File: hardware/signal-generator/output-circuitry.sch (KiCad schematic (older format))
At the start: 41 parts, among them U15 MCP4651-502E/ST, U16 AZ431AN-A, U17 AD8021ARZ, U18 MCP4551-103E/MS, U19 AD8021ARZ, U20 AD8021ARZ, U21 AD8021ARZ

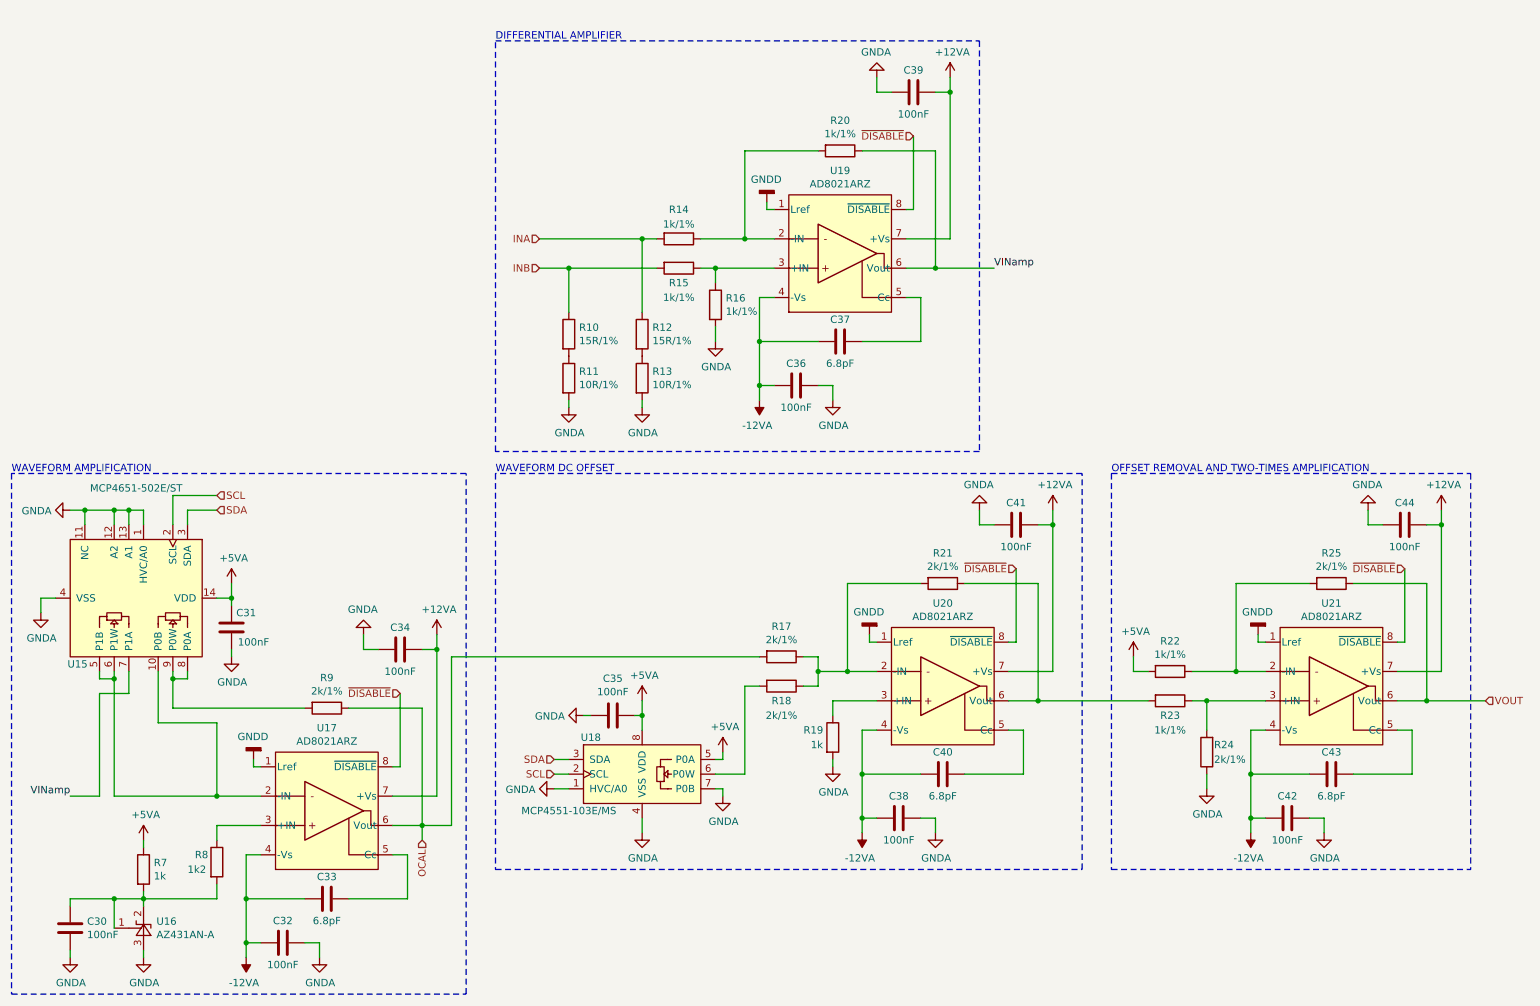
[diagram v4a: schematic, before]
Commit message: [Signal Generator] Rework output circuitry's waveform amplification stage
The previous design of the waveform amplification stage which utilized
a digital potentiometer to regulate gain control was flawed due to the
latter. The digital potentiometer's bandwidth is 2MHz which does not
fulfill the requirements of the circuit - the output stages may need to
accommodate for signals with frequencies in the tens of MHz.

This commit proposes a new design which uses JFET transistors as voltage
controlled variable resistors. In case this new design is unsuccessful,
the gain of the waveform amplification output stage may be regulated via
a mechanical potentiometer.
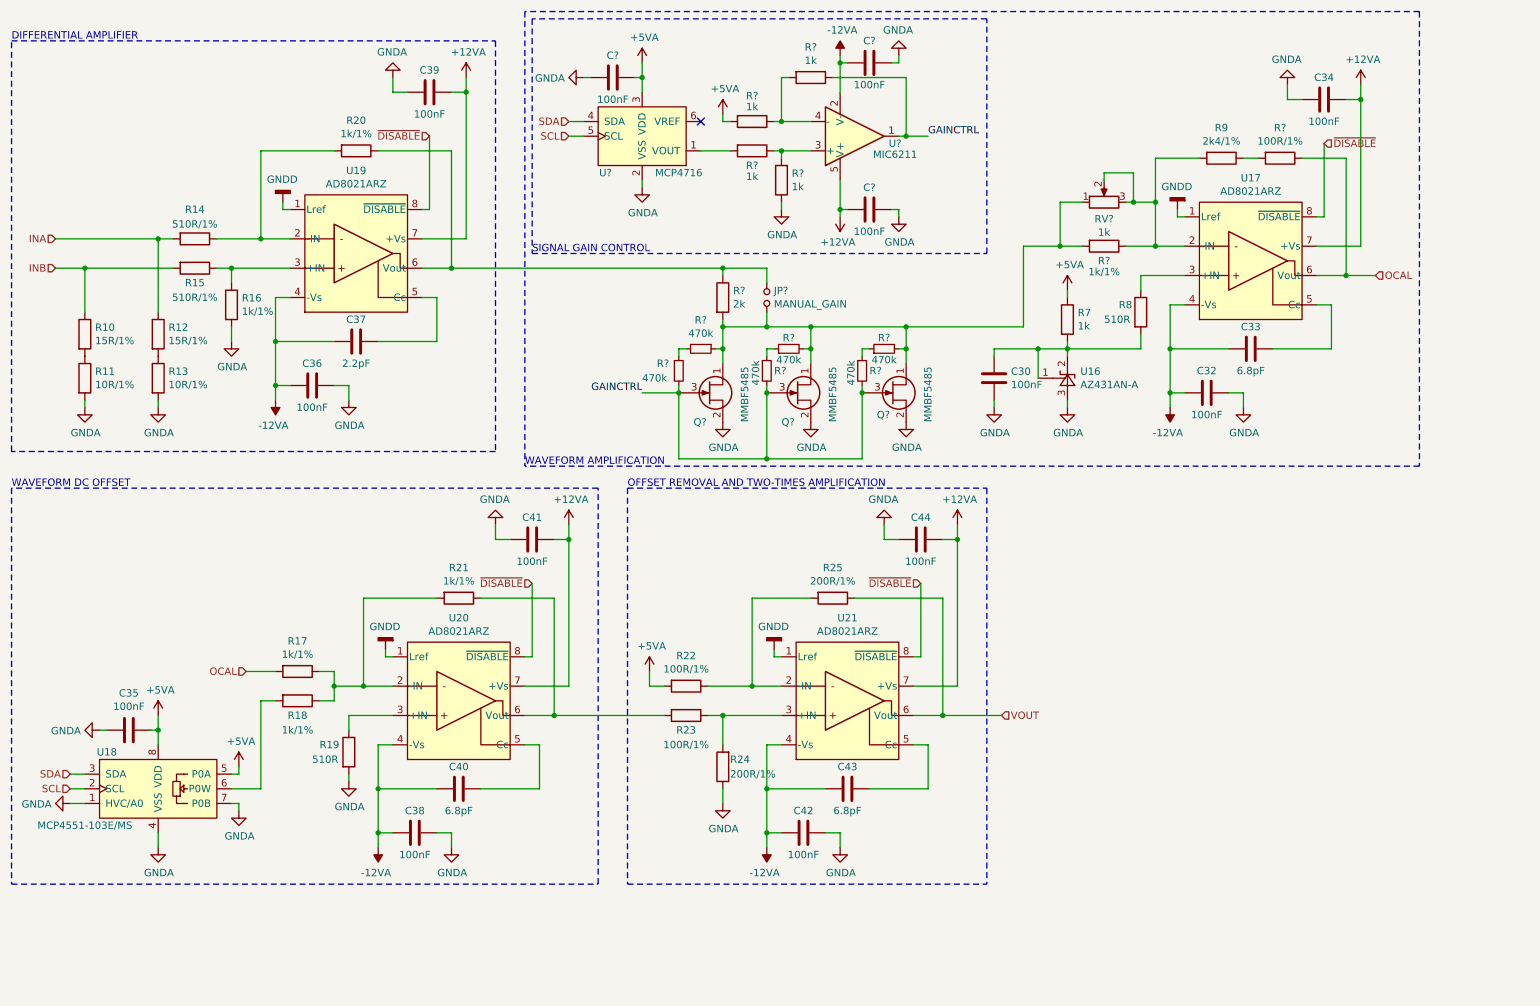
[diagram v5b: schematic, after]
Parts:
- removed C31: 100nF, Capacitors_SMD:C_0805_HandSoldering, symbol Device:C
- removed U15: MCP4651-502E/ST, Housings_SSOP:TSSOP-14_4.4x5mm_Pitch0.65mm, symbol ulib_Digital_Potentiometers:MCP4651-ST
- added C? (x3): 100nF, Capacitors_SMD:C_0805_HandSoldering, symbol Device:C
- added JP?: MANUAL_GAIN, symbol Device:Jumper_NO_Small
- added Q? (x3): MMBF5485, TO_SOT_Packages_SMD:SOT-23_Handsoldering, symbol ulib_MY_Transistor_FET:MMBF5485
- added R?: 1k/1%, symbol Device:R
- added R?: 2k, symbol Device:R
- added R? (x4): 1k, symbol Device:R
- added R?: 100R/1%, Resistors_SMD:R_0805_HandSoldering, symbol Device:R
- added R? (x6): 470k, symbol Device:R_Small
- added RV?: 1k, symbol Device:R_POT
- added U?: MCP4716, TO_SOT_Packages_SMD:SOT-23-6_Handsoldering, symbol ulib_DACs:MCP4716
- added U?: MIC6211, TO_SOT_Packages_SMD:SOT-23-5_HandSoldering, symbol ulib_IC_Amplifiers:MIC6211
- C37: value 6.8pF -> 2.2pF
- R14, R15: value 1k/1% -> 510R/1%
- R17, R18, R21: value 2k/1% -> 1k/1%
- R19: value 1k -> 510R
- R22, R23: value 1k/1% -> 100R/1%
- R24, R25: value 2k/1% -> 200R/1%
- R8: value 1k2 -> 510R
- R9: value 2k/1% -> 2k4/1%
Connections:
- net +12VA: now also C?.2, U?.5 (V+)
- net +5VA: now also C?.1, R?.2, U?.3 (VDD)
- net -12VA: now also C?.2, U?.2 (V-)
- net GNDA: now also C?.1, C?.1, C?.2, Q?.2 (S), Q?.2 (S), Q?.2 (S), R?.1, U?.2 (VSS)
- net OCAL: now also R?.1; no longer R9.1
- net SCL: now also U?.5 (SCL)
- net SDA: now also U?.4 (SDA)
- net at U17.2 (-IN): now also R9.2, R?.1, RV?.2, RV?.3
- net VINamp: no longer names the net of R20.1, U19.6 (Vout)
- net VINamp: now also JP?.1, R?.1
- new net: R9.1, R?.2
- new net: JP?.2, Q?.1 (D), Q?.1 (D), Q?.1 (D), R?.1, R?.2, R?.2, R?.2, R?.2, RV?.1
- new net: R?.2, U?.1 (VOUT)
- new net: R?.1, R?.2, U?.3 (+)
- new net: R?.1, R?.2, U?.4 (-)
- new net: R?.1, R?.2
- new net: R?.1, R?.1 (x2)
- new net GAINCTRL: Q?.3 (G), Q?.3 (G), Q?.3 (G), R?.1, R?.2, R?.2, R?.2, U?.1
- no-connect marks 0 -> 1
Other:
- note added: "SIGNAL GAIN CONTROL"
- moved on the sheet: C30, C32, C33, C34, C35, C36, C37, C38, C39, C40, C41, C42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

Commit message: [Signal Generator] Restore PCB layout with new symbol annotations
The new components have been loaded in the PCB file.
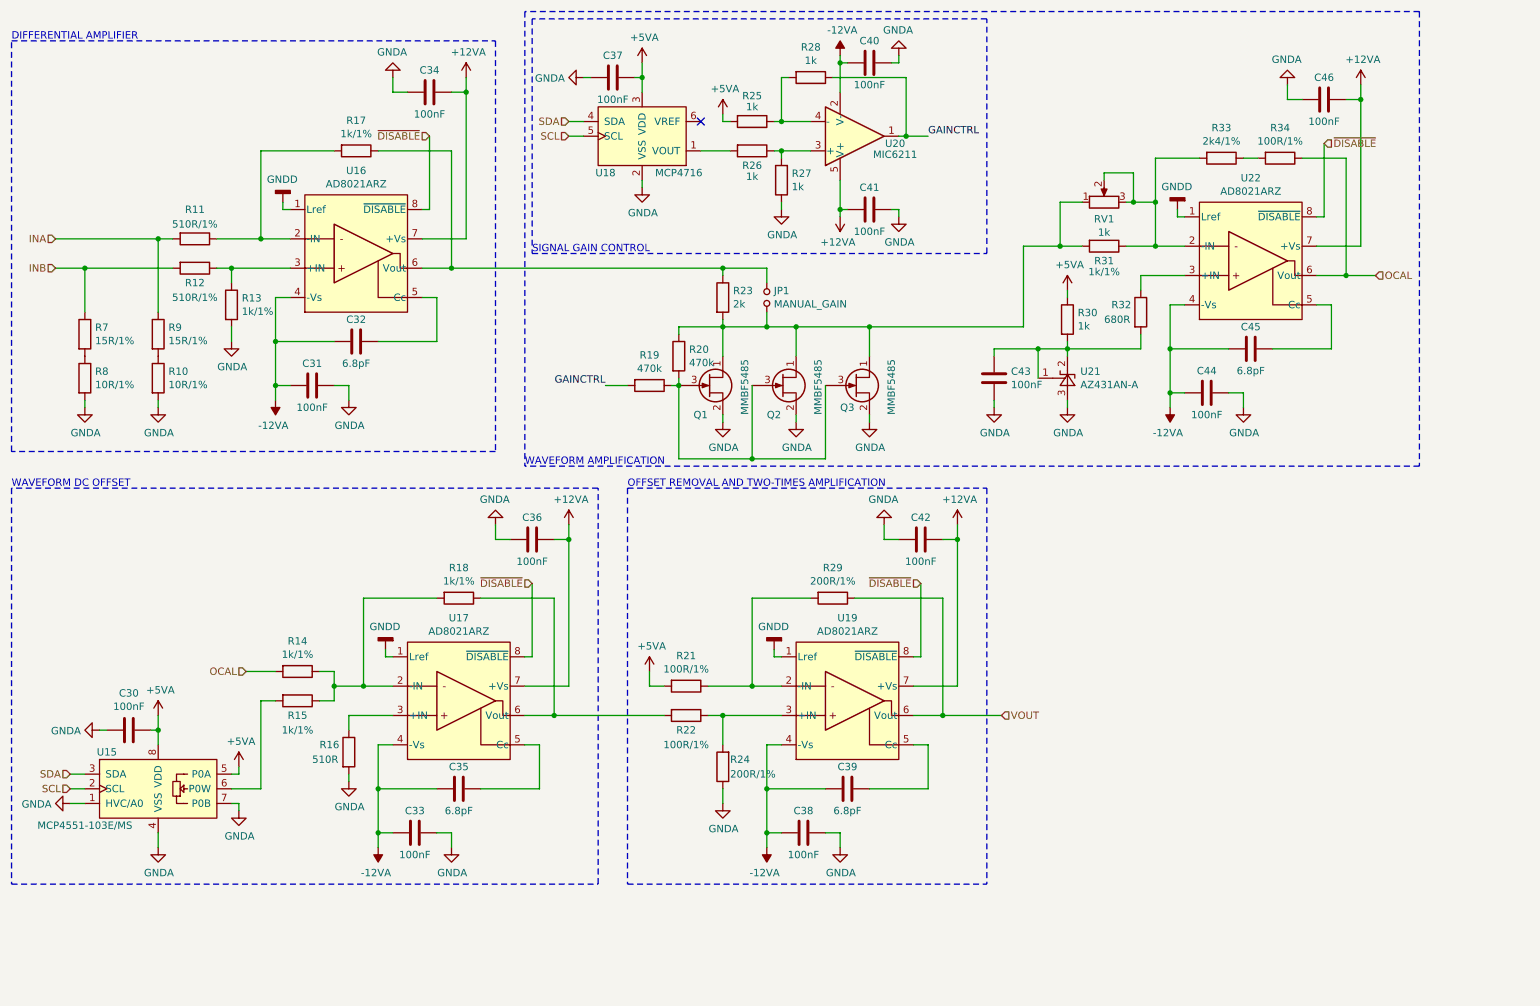
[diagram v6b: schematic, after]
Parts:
- removed R? (x6): 470k, symbol Device:R_Small
- added R19, R20: 470k, Resistors_SMD:R_0805_HandSoldering, symbol Device:R
- C32: renamed from C37; value 2.2pF -> 6.8pF
- JP1: renamed from JP?; footprint (none) -> Resistors_SMD:R_0805_HandSoldering
- R23, R25, R26, R27, R28, R31: renamed from R?; footprint (none) -> Resistors_SMD:R_0805_HandSoldering
- R32: renamed from R8; value 510R -> 680R
- RV1: renamed from RV?; footprint (none) -> Potentiometers:Potentiometer_Alps_RK163_Single_Vertical
- gave numbers to parts that had none: 9
- renumbered C35 to C30, C36 to C31, C38 to C33, C39 to C34, C40 to C35, C41 to C36, C42 to C38, C43 to C39, C44 to C42, C30 to C43, C32 to C44, C33 to C45, C34 to C46, R13 to R10, R14 to R11, R15 to R12, R16 to R13, R17 to R14, R18 to R15, R19 to R16, R20 to R17, R21 to R18, R22 to R21, R23 to R22, R25 to R29, R7 to R30, R9 to R33, R10 to R7, R11 to R8, R12 to R9, U18 to U15, U19 to U16, U20 to U17, U21 to U19, U16 to U21, U17 to U22
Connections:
- net GAINCTRL: now also R19.2; no longer Q1.3 (G), Q2.3 (G), Q3.3 (G)
- net at JP1.2, Q1.1 (D), Q2.1 (D)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: now also R20.1
- new net: Q1.3 (G), Q2.3 (G), Q3.3 (G), R19.1, R20.2
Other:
- moved on the sheet: Q1, Q2, Q3

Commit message: [Signal Generator] Layout output circuitry on PCB
Track lengths are kept to a minimum to facilitate the high-speed
analog signals traversing the output circuitry. As a result the layout
of these components is rather compact.
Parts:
- removed JP1: MANUAL_GAIN, Resistors_SMD:R_0805_HandSoldering, symbol Device:Jumper_NO_Small
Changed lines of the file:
@@
 	7750 2150 7750 2700
 $Comp
-L Device:Jumper_NO_Small JP1
+L Device:Jumper_NO_Small #JP1
 U 1 1 5E73BD80
 P 6000 2500
-F 0 "JP1" V 5954 2548 50  0000 L CNN
+F 0 "#JP1" V 5954 2548 50  0000 L CNN
 F 1 "MANUAL_GAIN" V 6045 2548 50  0000 L CNN
 F 2 "Resistors_SMD:R_0805_HandSoldering" H 6000 2500 50  0001 C CNN
